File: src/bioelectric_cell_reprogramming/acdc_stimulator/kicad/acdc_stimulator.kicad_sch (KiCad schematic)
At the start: 67 parts, among them IC1 AD9833BRM-REEL7, IC2 AD5122BCPZ10-RL7, J1 Screw_Terminal_01x02, J2 Conn_ARM_SWD_TagConnect_TC203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, J3 USB_C_Receptacle_USB2.0_14P, J4 S4B-PH-SM4-TB, J5 IPL1-102-01-L-S-K, J6 Screw_Terminal_01x02, J7 IPL1-102-01-L-S-K, Q1 BSZ096N10LS5ATMA1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

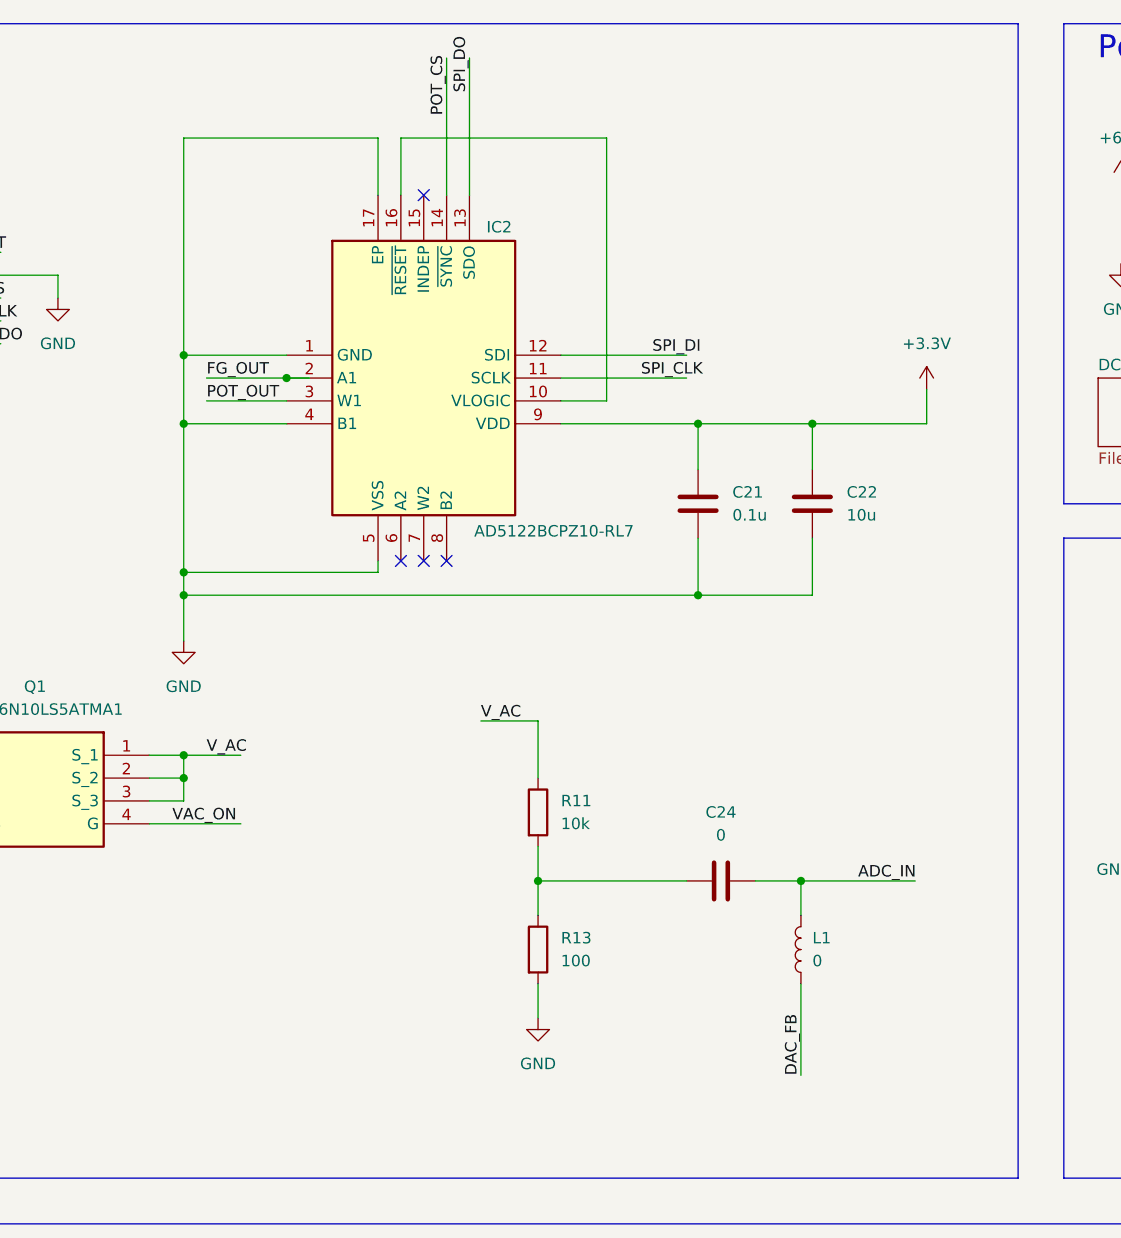
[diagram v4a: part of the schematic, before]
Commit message: ci: replaced digital pot with one thats available in JLCPCB
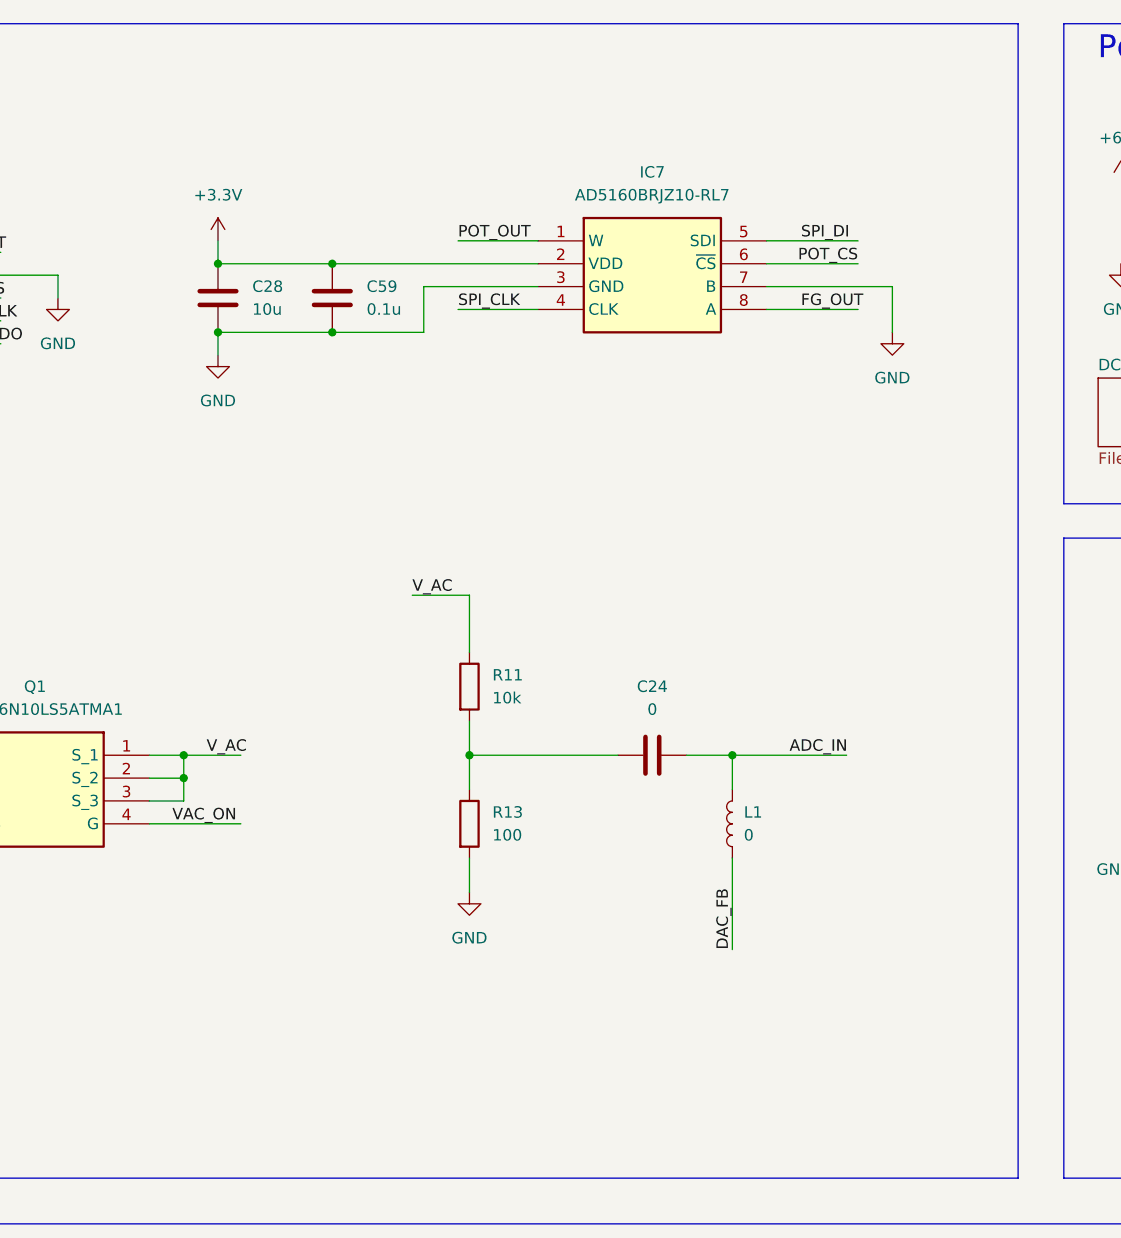
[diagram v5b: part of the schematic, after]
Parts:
- removed C21: 0.1u, Capacitor_SMD:C_0402_1005Metric, symbol Device:C
- removed C22: 10u, Capacitor_SMD:C_0603_1608Metric, symbol Device:C
- removed IC2: AD5122BCPZ10-RL7, AD5122BCPZ10-RL7:QFN50P300X300X80-17N-D, symbol AD5122BCPZ10-RL7:AD5122BCPZ10-RL7
- added C28: 10u, Capacitor_SMD:C_0603_1608Metric, symbol Device:C
- added C59: 0.1u, Capacitor_SMD:C_0402_1005Metric, symbol Device:C
- added IC7: AD5160BRJZ10-RL7, SOT65P280X145-8N, symbol AD5160BRJZ10-RL7:AD5160BRJZ10-RL7
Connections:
- net +3.3V: now also C28.1, C59.1, IC7.2 (VDD)
- net FG_OUT: now also IC7.8 (A)
- net GND: now also C28.2, C59.2, IC7.3 (GND), IC7.7 (B)
- net POT_CS: now also IC7.6 (~{CS})
- net POT_OUT: now also IC7.1 (W)
- net SPI_CLK: now also IC7.4 (CLK)
- net SPI_DI: now also IC7.5 (SDI)
- no-connect marks 27 -> 23
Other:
- moved on the sheet: C24, L1, R11, R13

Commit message: ci: build files for v0.0.2 generated
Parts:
- added R35: 72k, Resistor_SMD:R_0603_1608Metric, symbol Device:R
- R14: value 172k -> 100k; Distributor Link https://jlcpcb.com/partdetail/Yageo-RT0603BRD07172KL/C861162 -> https://jlcpcb.com/partdetail/Yageo-RC0603FR07100KL/C14675; Manufacturer Part Number RT0603BRD07172KL -> RC0603FR-07100KL
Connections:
- net V_DC: now also R35.2; no longer R14.2
- new net: R14.2, R35.1
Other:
- moved on the sheet: R14
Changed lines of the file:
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@@
 	(paper "A3")
 	(junction
+		(at 232.41 109.22)
+		(diameter 0)
+		(color 0 0 0 0)
+	)
+	(junction
 		(at 85.09 170.18)
 		(diameter 0)
@@
 	)
 	(junction
-		(at 278.13 114.3)
-		(diameter 0)
-		(color 0 0 0 0)
-	)
-	(junction
 		(at 34.29 176.53)
 		(diameter 0)
@@
 	)
 	(junction
-		(at 231.14 109.22)
-		(diameter 0)
-		(color 0 0 0 0)
-	)
-	(junction
 		(at 110.49 41.91)
 		(diameter 0)
@@
 	)
 	(junction
+		(at 274.32 114.3)
+		(diameter 0)
+		(color 0 0 0 0)
+	)
+	(junction
 		(at 323.85 173.99)
 		(diameter 0)
@@
 	(wire
 		(pts
+			(xy 232.41 109.22) (xy 240.03 109.22)
+		)
+		(stroke
+			(width 0)
+			(type default)
+		)
+	)
+	(wire
+		(pts
 			(xy 53.34 200.66) (xy 48.26 200.66)
 		)
@@
 	(wire
 		(pts
+			(xy 250.19 90.17) (xy 256.54 90.17)
+		)
+		(stroke
+			(width 0)
+			(type default)
+		)
+	)
+	(wire
+		(pts
 			(xy 133.35 44.45) (xy 133.35 49.53)
 		)
@@
 	(wire
 		(pts
-			(xy 257.81 90.17) (xy 278.13 90.17)
-		)
-		(stroke
-			(width 0)
-			(type default)
-		)
-	)
-	(wire
-		(pts
 			(xy 128.27 207.01) (xy 162.56 207.01)
 		)
@@
 	(wire
 		(pts
-			(xy 231.14 90.17) (xy 250.19 90.17)
+			(xy 232.41 90.17) (xy 242.57 90.17)
 		)
 		(stroke
@@
 	(wire
 		(pts
-			(xy 177.8 194.31) (xy 181.61 194.31)
+			(xy 264.16 90.17) (xy 274.32 90.17)
 		)
 		(stroke
@@
 	(wire
 		(pts
-			(xy 370.84 97.79) (xy 370.84 100.33)
+			(xy 177.8 194.31) (xy 181.61 194.31)
 		)
 		(stroke
@@
 	(wire
 		(pts
-			(xy 162.56 96.52) (xy 167.64 96.52)
+			(xy 370.84 97.79) (xy 370.84 100.33)
 		)
 		(stroke
@@
 	(wire
 		(pts
-			(xy 231.14 109.22) (xy 240.03 109.22)
+			(xy 162.56 96.52) (xy 167.64 96.52)
 		)
 		(stroke
@@
 	(wire
 		(pts
-			(xy 278.13 90.17) (xy 278.13 114.3)
+			(xy 274.32 90.17) (xy 274.32 114.3)
 		)
 		(stroke
@@
 	(wire
 		(pts
-			(xy 228.6 109.22) (xy 231.14 109.22)
+			(xy 228.6 109.22) (xy 232.41 109.22)
 		)
 		(stroke
@@
 	(wire
 		(pts
-			(xy 278.13 114.3) (xy 287.02 114.3)
-		)
-		(stroke
-			(width 0)
-			(type default)
-		)
-	)
-	(wire
-		(pts
-			(xy 231.14 109.22) (xy 231.14 90.17)
+			(xy 232.41 109.22) (xy 232.41 90.17)
 		)
 		(stroke
@@
 	(wire
 		(pts
-			(xy 266.7 114.3) (xy 278.13 114.3)
+			(xy 266.7 114.3) (xy 274.32 114.3)
 		)
 		(stroke
@@
 	(wire
 		(pts
+			(xy 274.32 114.3) (xy 287.02 114.3)
+		)
+		(stroke
+			(width 0)
+			(type default)
+		)
+	)
+	(wire
+		(pts
 			(xy 140.97 226.06) (xy 140.97 228.6)
 		)
@@
 	(symbol
 		(lib_id "Device:R")
-		(at 254 90.17 90)
+		(at 246.38 90.17 90)
 		(unit 1)
 		(exclude_from_sim no)
@@
 		(fields_autoplaced yes)
 		(property "Reference" "R14"
-			(at 254 83.82 90)
+			(at 246.38 83.82 90)
 			(effects
 				(font
@@
 			)
 		)
-		(property "Value" "172k"
-			(at 254 86.36 90)
+		(property "Value" "100k"
+			(at 246.38 86.36 90)
 			(effects
 				(font
@@
 		)
 		(property "Footprint" "Resistor_SMD:R_0603_1608Metric"
-			(at 254 91.948 90)
+			(at 246.38 91.948 90)
 			(effects
 				(font
@@
 		)
 		(property "Datasheet" "~"
-			(at 254 90.17 0)
+			(at 246.38 90.17 0)
 			(effects
 				(font
@@
 		)
 		(property "Description" "Resistor"
-			(at 254 90.17 0)
+			(at 246.38 90.17 0)
 			(effects
 				(font
@@
 			)
 		)
-		(property "Distributor Link" "https://jlcpcb.com/partdetail/Yageo-RT0603BRD07172KL/C861162"
-			(at 254 90.17 0)
+		(property "Distributor Link" "https://jlcpcb.com/partdetail/Yageo-RC0603FR07100KL/C14675"
+			(at 246.38 90.17 0)
 			(effects
 				(font
@@
 		)
 		(property "Manufacturer" "YAGEO"
-			(at 254 90.17 0)
+			(at 246.38 90.17 0)
 			(effects
 				(font
@@
 			)
 		)
-		(property "Manufacturer Part Number" "RT0603BRD07172KL"
-			(at 254 90.17 0)
+		(property "Manufacturer Part Number" "RC0603FR-07100KL"
+			(at 246.38 90.17 0)
 			(effects
 				(font
@@
 		)
 		(property "JLCPCB Part #" ""
-			(at 254 90.17 0)
+			(at 246.38 90.17 0)
 			(effects
 				(font
@@
 					(unit 1)
 				)
+			)
+		)
+	)
+	(symbol
+		(lib_id "Device:R")
+		(at 260.35 90.17 90)
+		(unit 1)
+		(exclude_from_sim no)
+		(in_bom yes)
+		(on_board yes)
+		(dnp no)
+		(fields_autoplaced yes)
+		(property "Reference" "R35"
+			(at 260.35 83.82 90)
+			(effects
+				(font
+					(size 1.27 1.27)
+				)
+			)
+		)
+		(property "Value" "72k"
+			(at 260.35 86.36 90)
+			(effects
+				(font
+					(size 1.27 1.27)
+				)
+			)
+		)
+		(property "Footprint" "Resistor_SMD:R_0603_1608Metric"
+			(at 260.35 91.948 90)
+			(effects
+				(font
+					(size 1.27 1.27)
+				)
+				(hide yes)
+			)
+		)
+		(property "Datasheet" "~"
+			(at 260.35 90.17 0)
+			(effects
+				(font
+					(size 1.27 1.27)
+				)
+				(hide yes)
+			)
+		)
+		(property "Description" "Resistor"
+			(at 260.35 90.17 0)
+			(effects
+				(font
+					(size 1.27 1.27)
+				)
+				(hide yes)
+			)
+		)
+		(property "Distributor Link" "https://jlcpcb.com/partdetail/VikingTech-AR03BTCX7202N/C2828635"
+			(at 260.35 90.17 0)
+			(effects
+				(font
+					(size 1.27 1.27)
+				)
+				(hide yes)
+			)
+		)
+		(property "Manufacturer" "Viking Tech"
+			(at 260.35 90.17 0)
+			(effects
+				(font
+					(size 1.27 1.27)
+				)
+				(hide yes)
+			)
+		)
+		(property "Manufacturer Part Number" "AR03BTCX7202N"
+			(at 260.35 90.17 0)
+			(effects
+				(font
+					(size 1.27 1.27)
+				)
+				(hide yes)
+			)
+		)
+		(property "JLCPCB Part #" ""
+			(at 260.35 90.17 0)
+			(effects
+				(font
+					(size 1.27 1.27)
+				)
+				(hide yes)
+			)
+		)
+		(pin "1"
+		)
+		(pin "2"
+		)
+		(instances
+			(project "acdc_stimulator"
+				(path "/ec70e9f6-566f-44ea-8141-5580f51beca4"
+					(reference "R35")
+					(unit 1)
+				)

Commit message: ci: v0.0.3 manufacturing files uploaded
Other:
- removed sheet 60_to_3V3_converter
- removed sheet 60_to_5V_converter
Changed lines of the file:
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@@
 					(size 1.27 1.27)
 				)
-				(hide yes)
 			)
 		)
@@
 	)
 	(sheet
-		(at 292.1 49.53)
-		(size 29.21 13.97)
-		(fields_autoplaced yes)
-		(stroke
-			(width 0.1524)
-			(type solid)
-		)
-		(fill
-			(color 0 0 0 0.0000)
-		)
-		(property "Sheetname" "60_to_5V_converter"
-			(at 292.1 48.8184 0)
-			(effects
-				(font
-					(size 1.27 1.27)
-				)
-				(justify left bottom)
-			)
-		)
-		(property "Sheetfile" "60_to_5V_converter.kicad_sch"
-			(at 292.1 64.0846 0)
-			(effects
-				(font
-					(size 1.27 1.27)
-				)
-				(justify left top)
-			)
-		)
-		(instances
-			(project "acdc_stimulator"
-				(path "/ec70e9f6-566f-44ea-8141-5580f51beca4"
-					(page "9")
-				)
-			)
-		)
-	)
-	(sheet
 		(at 208.28 54.61)
 		(size 27.94 7.62)
@@
 				)
 			)
-		)
-	)
-	(sheet
-		(at 331.47 49.53)
-		(size 29.21 13.97)
-		(fields_autoplaced yes)
-		(stroke
-			(width 0.1524)
-			(type solid)
-		)
-		(fill
-			(color 0 0 0 0.0000)
-		)
-		(property "Sheetname" "60_to_3V3_converter"
-			(at 331.47 48.8184 0)
-			(effects
-				(font
-					(size 1.27 1.27)
-				)
-				(justify left bottom)
-			)
-		)
-		(property "Sheetfile" "60_to_3V3_converter.kicad_sch"
-			(at 331.47 64.0846 0)
-			(effects
-				(font
-					(size 1.27 1.27)
-				)
-				(justify left top)
-			)
-		)
-		(instances
-			(project "acdc_stimulator"
-				(path "/ec70e9f6-566f-44ea-8141-5580f51beca4"
-					(page "10")
-				)
-			)

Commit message: fix: updated mismatched cap packages
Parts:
- C17, C6: footprint Capacitor_SMD:C_0402_1005Metric -> Capacitor_SMD:C_0201_0603Metric
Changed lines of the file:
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@@
 			)
 		)
-		(property "Footprint" "Capacitor_SMD:C_0402_1005Metric"
+		(property "Footprint" "Capacitor_SMD:C_0201_0603Metric"
 			(at 134.3152 167.64 0)
 			(effects
@@
 			)
 		)
-		(property "Footprint" "Capacitor_SMD:C_0402_1005Metric"
+		(property "Footprint" "Capacitor_SMD:C_0201_0603Metric"
 			(at 43.18 29.5148 0)
 			(effects
